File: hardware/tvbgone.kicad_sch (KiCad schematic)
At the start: 6 parts, among them Q1 BS170, U1 XIAO-ESP32-S6, U2 TSOP382xx

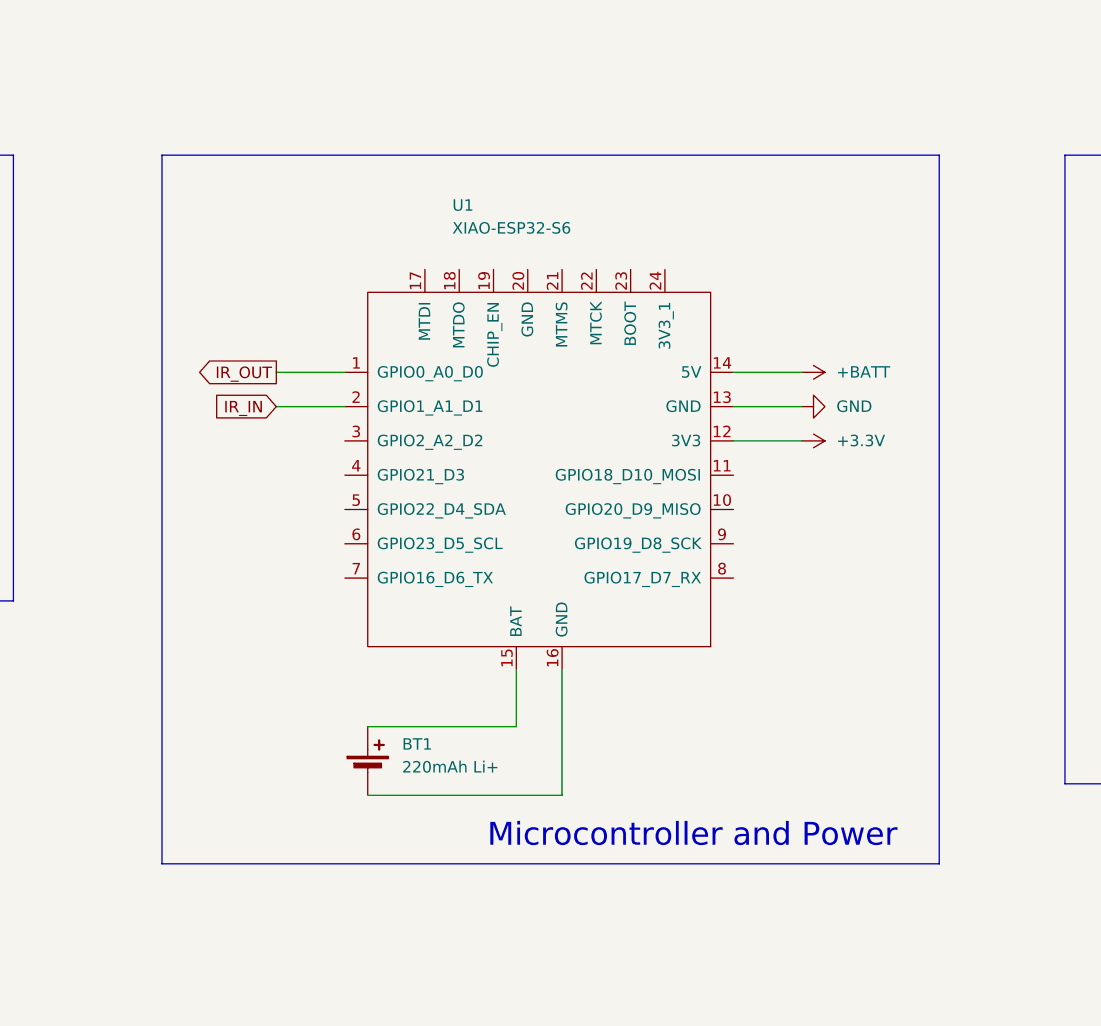
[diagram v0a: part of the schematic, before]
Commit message: Added loading of captured codes.
Also move button to GPIO 2.
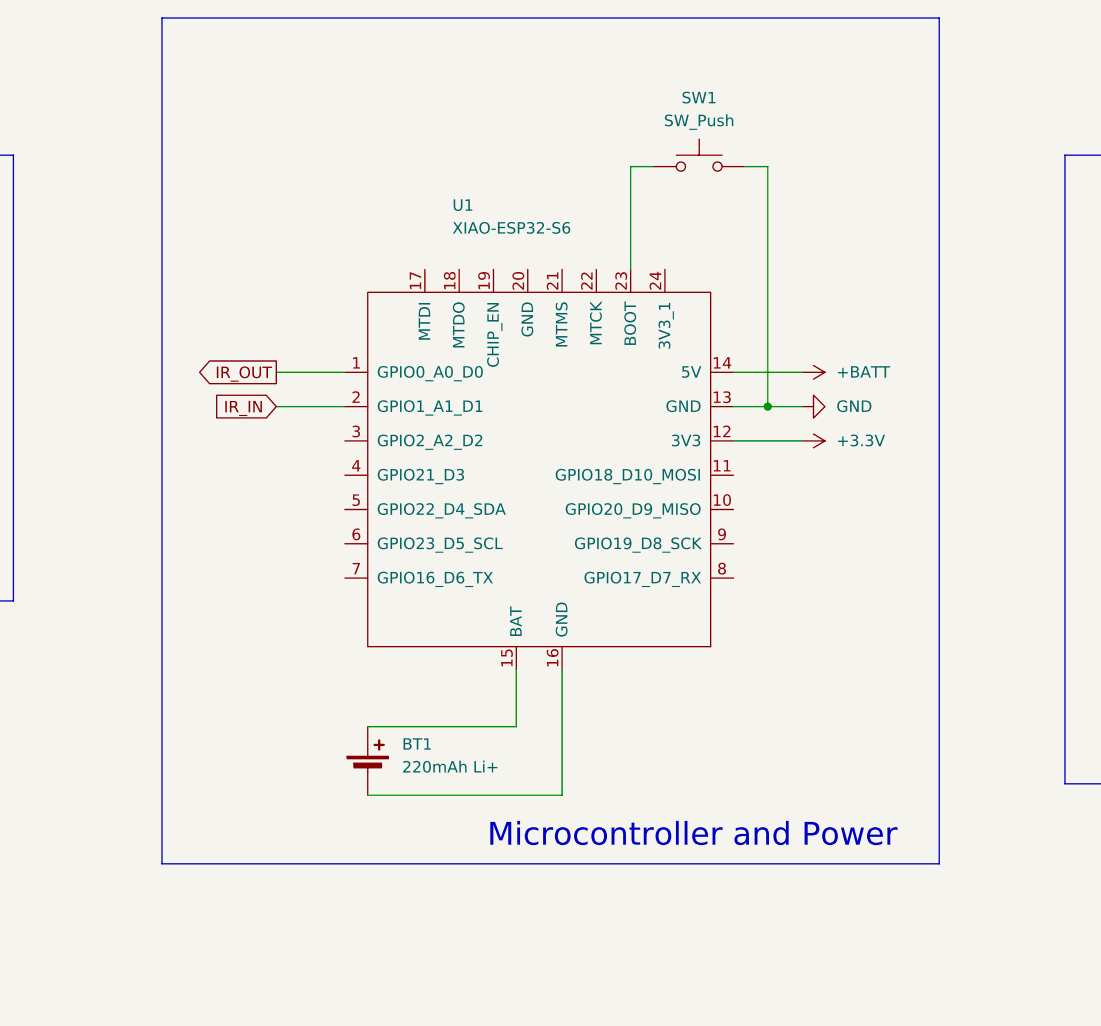
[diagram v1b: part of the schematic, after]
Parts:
- added SW1: SW_Push, symbol Switch:SW_Push
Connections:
- net GND: now also SW1.2
- net at U1.23 (BOOT): now also SW1.1
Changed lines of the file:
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@@
 	)
 	(rectangle
-		(start 91.44 71.12)
+		(start 91.44 55.88)
 		(end 177.8 149.86)
 		(stroke
@@
 		)
 	)
+	(junction
+		(at 158.75 99.06)
+		(diameter 0)
+		(color 0 0 0 0)
+	)
+	(wire
+		(pts
+			(xy 146.05 72.39) (xy 143.51 72.39)
+		)
+		(stroke
+			(width 0)
+			(type default)
+		)
+	)
 	(wire
 		(pts
@@
 	(wire
 		(pts
+			(xy 156.21 72.39) (xy 158.75 72.39)
+		)
+		(stroke
+			(width 0)
+			(type default)
+		)
+	)
+	(wire
+		(pts
 			(xy 220.98 82.55) (xy 220.98 88.9)
 		)
@@
 	(wire
 		(pts
+			(xy 143.51 72.39) (xy 143.51 83.82)
+		)
+		(stroke
+			(width 0)
+			(type default)
+		)
+	)
+	(wire
+		(pts
 			(xy 220.98 107.95) (xy 220.98 113.03)
 		)
@@
 	(wire
 		(pts
-			(xy 154.94 99.06) (xy 162.56 99.06)
+			(xy 154.94 99.06) (xy 158.75 99.06)
 		)
 		(stroke
@@
 	(wire
 		(pts
+			(xy 158.75 99.06) (xy 162.56 99.06)
+		)
+		(stroke
+			(width 0)
+			(type default)
+		)
+	)
+	(wire
+		(pts
 			(xy 130.81 134.62) (xy 130.81 128.27)
 		)
@@
 		(pts
 			(xy 154.94 102.87) (xy 162.56 102.87)
+		)
+		(stroke
+			(width 0)
+			(type default)
+		)
+	)
+	(wire
+		(pts
+			(xy 158.75 72.39) (xy 158.75 99.06)
 		)
 		(stroke
@@
 					(unit 1)
 				)
+			)
+		)
+	)
+	(symbol
+		(lib_id "Switch:SW_Push")
+		(at 151.13 72.39 0)
+		(unit 1)
+		(exclude_from_sim no)
+		(in_bom yes)
+		(on_board yes)
+		(dnp no)
+		(fields_autoplaced yes)
+		(property "Reference" "SW1"
+			(at 151.13 64.77 0)
+			(effects
+				(font
+					(size 1.27 1.27)
+				)
+			)
+		)
+		(property "Value" "SW_Push"
+			(at 151.13 67.31 0)
+			(effects
+				(font
+					(size 1.27 1.27)
+				)
+			)
+		)
+		(property "Footprint" ""
+			(at 151.13 67.31 0)
+			(effects
+				(font
+					(size 1.27 1.27)
+				)
+				(hide yes)
+			)
+		)
+		(property "Datasheet" "~"
+			(at 151.13 67.31 0)
+			(effects
+				(font
+					(size 1.27 1.27)
+				)
+				(hide yes)
+			)
+		)
+		(property "Description" "Push button switch, generic, two pins"
+			(at 151.13 72.39 0)
+			(effects
+				(font
+					(size 1.27 1.27)
+				)
+				(hide yes)
+			)
+		)
+		(pin "1"
+		)
+		(pin "2"
+		)
+		(instances
+			(project ""
+				(path "/58dc933f-1062-4738-8cb1-787931f6c816"
+					(reference "SW1")
+					(unit 1)
+				)

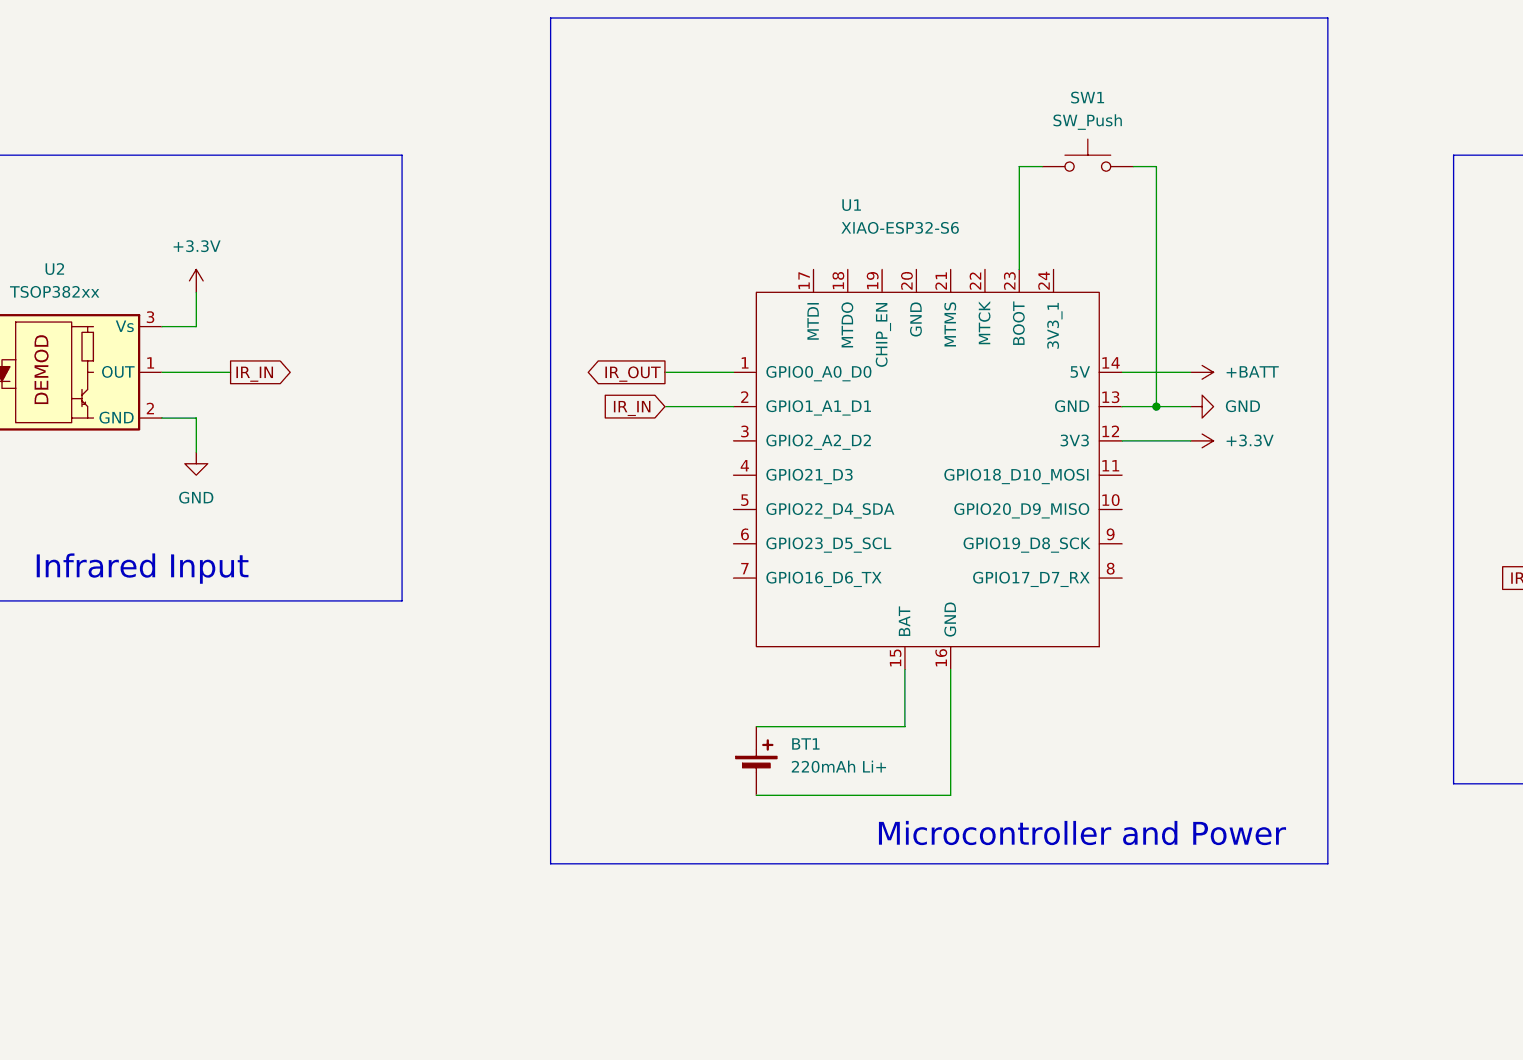
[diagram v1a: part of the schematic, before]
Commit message: Add deepsleep() support.
Also allow getting into capture from main loop by Ctrl-C.
Also add support for INPUT_POWER_PIN.
Also add PDF schematic.
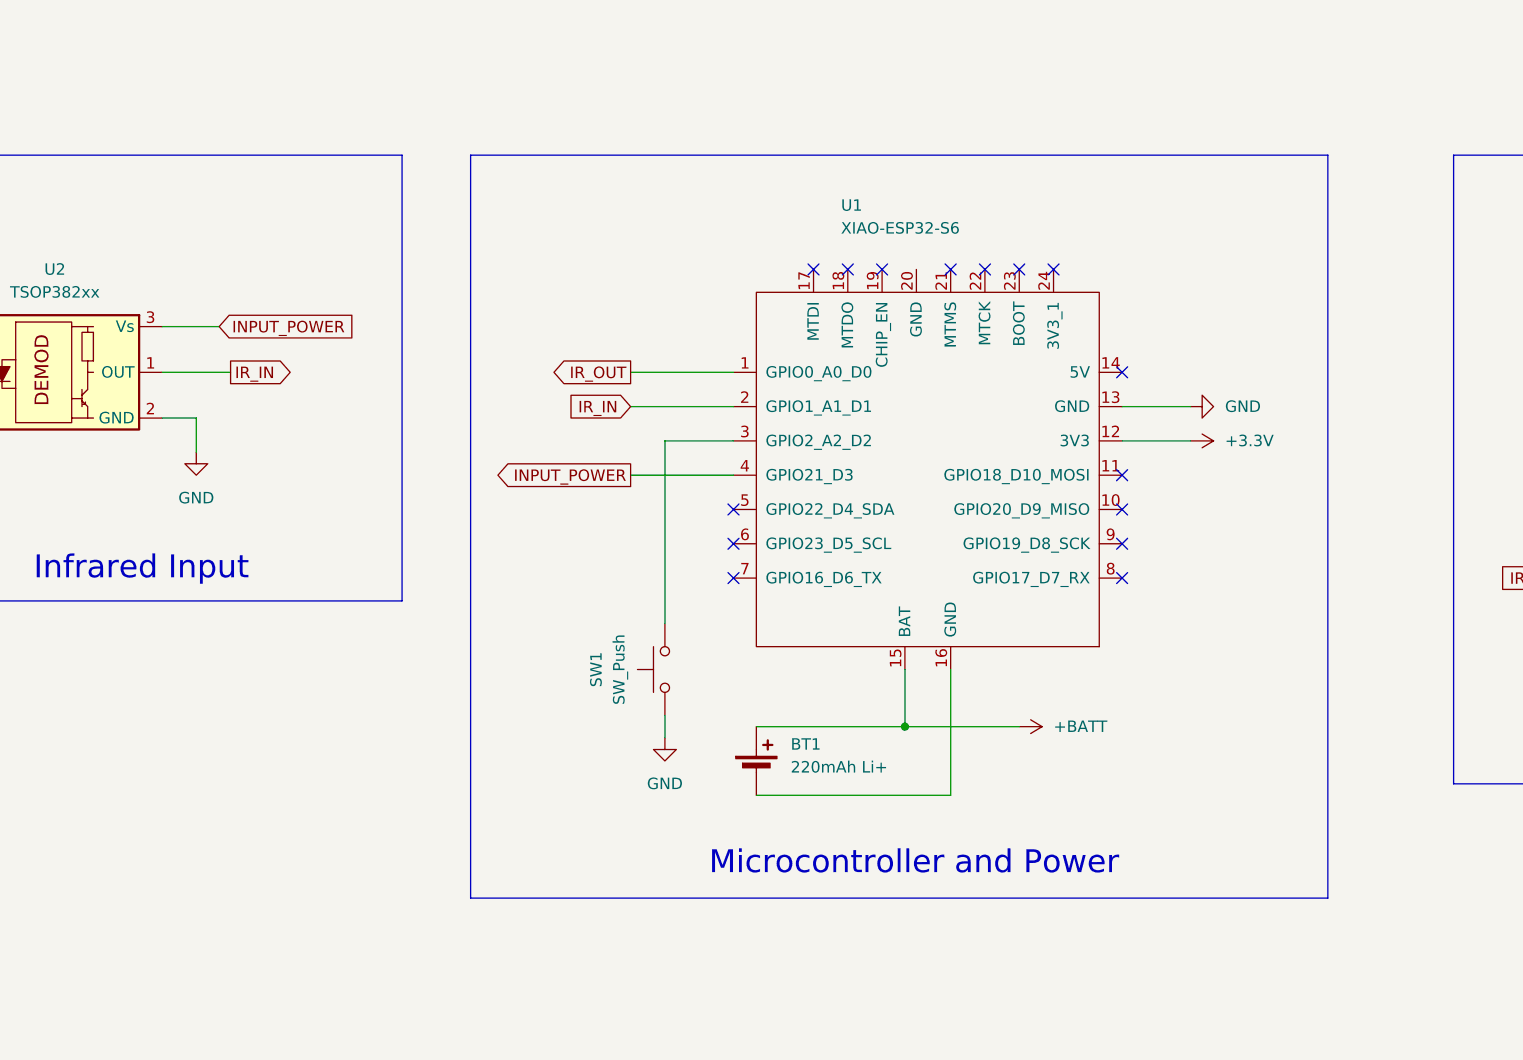
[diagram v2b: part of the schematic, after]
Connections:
- net +3.3V: no longer U2.3 (Vs)
- net +BATT: now also BT1.1 (+), U1.15 (BAT); no longer U1.14 (5V)
- net GND: now also SW1.1; no longer SW1.2
- net at U1.23 (BOOT): no longer SW1.1
- net at U1.3 (GPIO2_A2_D2): now also SW1.2
- net INPUT_POWER: now reaches U1.4 (GPIO21_D3)
- net INPUT_POWER: now also U2.3 (Vs)
- no-connect marks 0 -> 15
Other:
- moved on the sheet: SW1
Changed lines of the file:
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@@
 	)
 	(rectangle
-		(start 91.44 55.88)
-		(end 177.8 149.86)
+		(start 82.55 71.12)
+		(end 177.8 153.67)
 		(stroke
 			(width 0)
@@
 	(text "Microcontroller and Power"
 		(exclude_from_sim no)
-		(at 150.368 146.812 0)
+		(at 131.826 149.86 0)
 		(effects
 			(font
@@
 	)
 	(junction
-		(at 158.75 99.06)
+		(at 130.81 134.62)
 		(diameter 0)
 		(color 0 0 0 0)
 	)
-	(wire
-		(pts
-			(xy 146.05 72.39) (xy 143.51 72.39)
+	(no_connect
+		(at 120.65 83.82)
+	)
+	(no_connect
+		(at 154.94 110.49)
+	)
+	(no_connect
+		(at 128.27 83.82)
+	)
+	(no_connect
+		(at 139.7 83.82)
+	)
+	(no_connect
+		(at 111.76 114.3)
+	)
+	(no_connect
+		(at 154.94 118.11)
+	)
+	(no_connect
+		(at 111.76 118.11)
+	)
+	(no_connect
+		(at 124.46 83.82)
+	)
+	(no_connect
+		(at 135.89 83.82)
+	)
+	(no_connect
+		(at 154.94 114.3)
+	)
+	(no_connect
+		(at 111.76 110.49)
+	)
+	(no_connect
+		(at 147.32 83.82)
+	)
+	(no_connect
+		(at 143.51 83.82)
+	)
+	(no_connect
+		(at 154.94 106.68)
+	)
+	(no_connect
+		(at 154.94 95.25)
+	)
+	(wire
+		(pts
+			(xy 104.14 133.35) (xy 104.14 135.89)
 		)
 		(stroke
@@
 	(wire
 		(pts
-			(xy 156.21 72.39) (xy 158.75 72.39)
+			(xy 104.14 123.19) (xy 104.14 102.87)
 		)
 		(stroke
@@
 	(wire
 		(pts
-			(xy 104.14 99.06) (xy 111.76 99.06)
-		)
-		(stroke
-			(width 0)
-			(type default)
-		)
-	)
-	(wire
-		(pts
-			(xy 143.51 72.39) (xy 143.51 83.82)
+			(xy 100.33 99.06) (xy 111.76 99.06)
+		)
+		(stroke
+			(width 0)
+			(type default)
+		)
+	)
+	(wire
+		(pts
+			(xy 100.33 106.68) (xy 111.76 106.68)
+		)
+		(stroke
+			(width 0)
+			(type default)
+		)
+	)
+	(wire
+		(pts
+			(xy 104.14 102.87) (xy 111.76 102.87)
 		)
 		(stroke
@@
 	(wire
 		(pts
-			(xy 154.94 99.06) (xy 158.75 99.06)
+			(xy 154.94 99.06) (xy 162.56 99.06)
 		)
 		(stroke
@@
 	(wire
 		(pts
-			(xy 48.26 90.17) (xy 52.07 90.17)
-		)
-		(stroke
-			(width 0)
-			(type default)
-		)
-	)
-	(wire
-		(pts
-			(xy 158.75 99.06) (xy 162.56 99.06)
+			(xy 48.26 90.17) (xy 54.61 90.17)
 		)
 		(stroke
@@
 	(wire
 		(pts
-			(xy 52.07 90.17) (xy 52.07 86.36)
-		)
-		(stroke
-			(width 0)
-			(type default)
-		)
-	)
-	(wire
-		(pts
 			(xy 220.98 123.19) (xy 220.98 127)
 		)
@@
 	(wire
 		(pts
-			(xy 158.75 72.39) (xy 158.75 99.06)
-		)
-		(stroke
-			(width 0)
-			(type default)
-		)
-	)
-	(wire
-		(pts
-			(xy 162.56 95.25) (xy 154.94 95.25)
+			(xy 143.51 134.62) (xy 130.81 134.62)
 		)
 		(stroke
@@
 	(wire
 		(pts
-			(xy 104.14 95.25) (xy 111.76 95.25)
+			(xy 100.33 95.25) (xy 111.76 95.25)
 		)
 		(stroke
@@
 		)
 	)
-	(global_label "IR_IN"
+	(global_label "INPUT_POWER"
 		(shape input)
-		(at 104.14 99.06 180)
+		(at 54.61 90.17 0)
 		(fields_autoplaced yes)
 		(effects
@@
 				(size 1.27 1.27)
 			)
+			(justify left)
+		)
+		(property "Intersheetrefs" "${INTERSHEET_REFS}"
+			(at 70.5371 90.17 0)
+			(effects
+				(font
+					(size 1.27 1.27)
+				)
+				(justify left)
+				(hide yes)
+			)
+		)
+	)
+	(global_label "IR_IN"
+		(shape input)
+		(at 100.33 99.06 180)
+		(fields_autoplaced yes)
+		(effects
+			(font
+				(size 1.27 1.27)
+			)
 			(justify right)
 		)
 		(property "Intersheetrefs" "${INTERSHEET_REFS}"
-			(at 96.3771 99.06 0)
+			(at 92.5671 99.06 0)
 			(effects
 				(font
@@
 	(global_label "IR_OUT"
 		(shape output)
-		(at 104.14 95.25 180)
+		(at 100.33 95.25 180)
 		(fields_autoplaced yes)
 		(effects
@@
 		)
 		(property "Intersheetrefs" "${INTERSHEET_REFS}"
-			(at 94.6838 95.25 0)
+			(at 90.8738 95.25 0)
+			(effects
+				(font
+					(size 1.27 1.27)
+				)
+				(justify right)
+				(hide yes)
+			)
+		)
+	)
+	(global_label "INPUT_POWER"
+		(shape output)
+		(at 100.33 106.68 180)
+		(fields_autoplaced yes)
+		(effects
+			(font
+				(size 1.27 1.27)
+			)
+			(justify right)
+		)
+		(property "Intersheetrefs" "${INTERSHEET_REFS}"
+			(at 84.4029 106.68 0)
 			(effects
 				(font
@@
 	(symbol
 		(lib_id "Switch:SW_Push")
-		(at 151.13 72.39 0)
+		(at 104.14 128.27 90)
 		(unit 1)
 		(exclude_from_sim no)
@@
 		(fields_autoplaced yes)
 		(property "Reference" "SW1"
-			(at 151.13 64.77 0)
+			(at 96.52 128.27 0)
 			(effects
 				(font
@@
 		)
 		(property "Value" "SW_Push"
-			(at 151.13 67.31 0)
+			(at 99.06 128.27 0)
 			(effects
 				(font
@@
 		)
 		(property "Footprint" ""
-			(at 151.13 67.31 0)
+			(at 99.06 128.27 0)
 			(effects
 				(font
@@
 		)
 		(property "Datasheet" "~"
-			(at 151.13 67.31 0)
+			(at 99.06 128.27 0)
 			(effects
 				(font
@@
 		)
 		(property "Description" "Push button switch, generic, two pins"
-			(at 151.13 72.39 0)
+			(at 104.14 128.27 0)
 			(effects
 				(font
@@
 	)
 	(symbol
-		(lib_id "power:+3.3V")
-		(at 52.07 86.36 0)
-		(unit 1)
-		(exclude_from_sim no)
-		(in_bom yes)
-		(on_board yes)
-		(dnp no)
-		(fields_autoplaced yes)
-		(property "Reference" "#PWR03"
-			(at 52.07 90.17 0)
-			(effects
-				(font
-					(size 1.27 1.27)
-				)
-				(hide yes)
-			)
-		)
-		(property "Value" "+3.3V"
-			(at 52.07 81.28 0)
-			(effects
-				(font
-					(size 1.27 1.27)
-				)
-			)
-		)
-		(property "Footprint" ""
-			(at 52.07 86.36 0)
-			(effects
-				(font
-					(size 1.27 1.27)
-				)
-				(hide yes)
-			)
-		)
-		(property "Datasheet" ""
-			(at 52.07 86.36 0)
-			(effects
-				(font
-					(size 1.27 1.27)
-				)
-				(hide yes)
-			)
-		)
-		(property "Description" "Power symbol creates a global label with name \"+3.3V\""
-			(at 52.07 86.36 0)
-			(effects
-				(font
-					(size 1.27 1.27)
-				)
-				(hide yes)
-			)
-		)
-		(pin "1"
-		)
-		(instances
-			(project "tvbgone"
-				(path "/58dc933f-1062-4738-8cb1-787931f6c816"
-					(reference "#PWR03")
-					(unit 1)
-				)
-			)
-		)
-	)
-	(symbol
 		(lib_id "power:+BATT")
 		(at 220.98 82.55 0)
@@
 	)
 	(symbol
-		(lib_id "power:+BATT")
-		(at 162.56 95.25 270)
+		(lib_id "power:GND")
+		(at 104.14 135.89 0)
 		(unit 1)
 		(exclude_from_sim no)
@@
 		(dnp no)
 		(fields_autoplaced yes)
+		(property "Reference" "#PWR08"
+			(at 104.14 142.24 0)
+			(effects
+				(font
+					(size 1.27 1.27)
+				)
+				(hide yes)
+			)
+		)
+		(property "Value" "GND"
+			(at 104.14 140.97 0)
+			(effects
+				(font
+					(size 1.27 1.27)
+				)
+			)
+		)
+		(property "Footprint" ""
+			(at 104.14 135.89 0)
+			(effects
+				(font
+					(size 1.27 1.27)
+				)
+				(hide yes)
+			)
+		)
+		(property "Datasheet" ""
+			(at 104.14 135.89 0)
+			(effects
+				(font
+					(size 1.27 1.27)
+				)
+				(hide yes)
+			)
+		)
+		(property "Description" "Power symbol creates a global label with name \"GND\" , ground"
+			(at 104.14 135.89 0)
+			(effects
+				(font
+					(size 1.27 1.27)
+				)
+				(hide yes)
+			)
+		)
+		(pin "1"
+		)
+		(instances
+			(project "tvbgone"
+				(path "/58dc933f-1062-4738-8cb1-787931f6c816"
+					(reference "#PWR08")
+					(unit 1)
+				)
+			)
+		)
+	)
+	(symbol
+		(lib_id "power:+BATT")
+		(at 143.51 134.62 270)
+		(unit 1)
+		(exclude_from_sim no)
+		(in_bom yes)
+		(on_board yes)
+		(dnp no)
+		(fields_autoplaced yes)
 		(property "Reference" "#PWR06"
-			(at 158.75 95.25 0)
+			(at 139.7 134.62 0)
 			(effects
 				(font
@@
 		)
 		(property "Value" "+BATT"
-			(at 166.37 95.2499 90)
+			(at 147.32 134.6199 90)
 			(effects
 				(font
@@
 		)
 		(property "Footprint" ""
-			(at 162.56 95.25 0)
+			(at 143.51 134.62 0)
 			(effects
 				(font
@@
 		)
 		(property "Datasheet" ""
-			(at 162.56 95.25 0)
+			(at 143.51 134.62 0)
 			(effects
 				(font
@@
 		)
 		(property "Description" "Power symbol creates a global label with name \"+BATT\""
-			(at 162.56 95.25 0)
-			(effects
-				(font
+			(at 143.51 134.62 0)
+			(effects
+				(font
